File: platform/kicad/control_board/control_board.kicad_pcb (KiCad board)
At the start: 2 copper layers, 81.5 x 131.5 mm, 63 parts, among them J1 DHT22, J10 ADC1,7, J11 Qwiic JST, J12 Conn_01x03, J13 PJ-002A, J14 ROUTER 24V, J15 24V/5V OUT, J16 Conn_01x05_Pin, J2 DS18B20, J3 Conn_01x03, J4 24V IN, J5 USB4120-03-C_REVA, J8 UART, J9 ADC1,6, K1 LCA717, K2 LCA717, K3 LCA717, K4 LCA717, U1 ESP32-DevKitC, U2 ACS722xLCTR-20AU, U3 AP63205WU-7

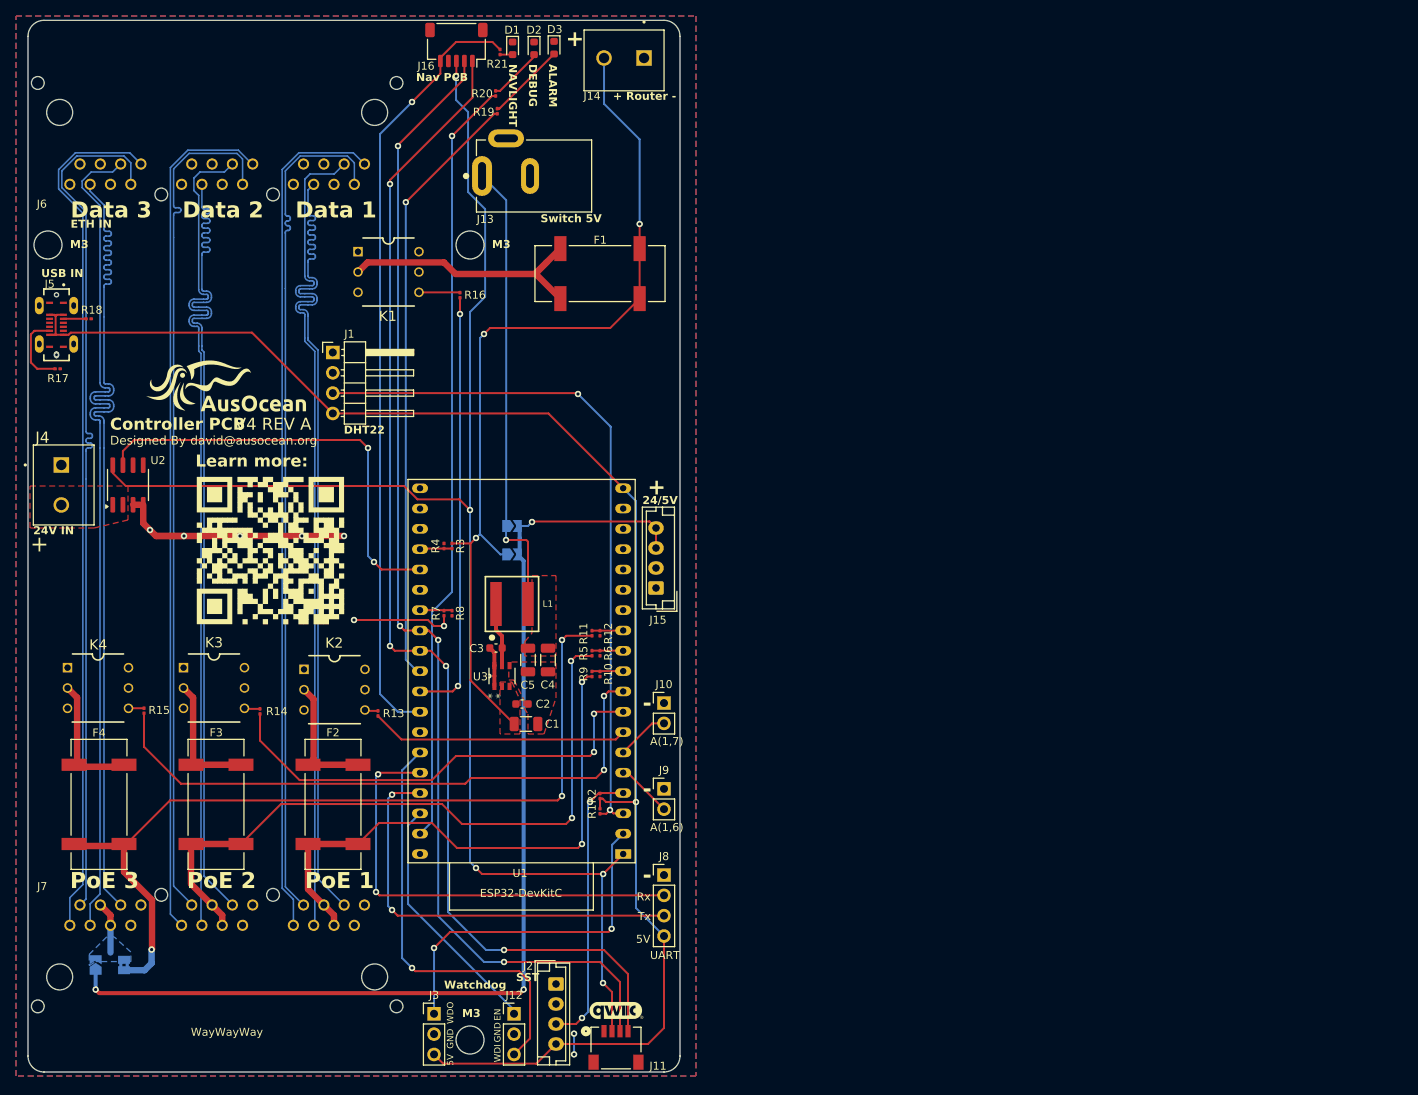
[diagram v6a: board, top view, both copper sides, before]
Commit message: Control_PCB v4 revB: Finalised Design
This change updates the controller PCB to a finalised state, only requiring
finishing touches to be made for manufacturing.
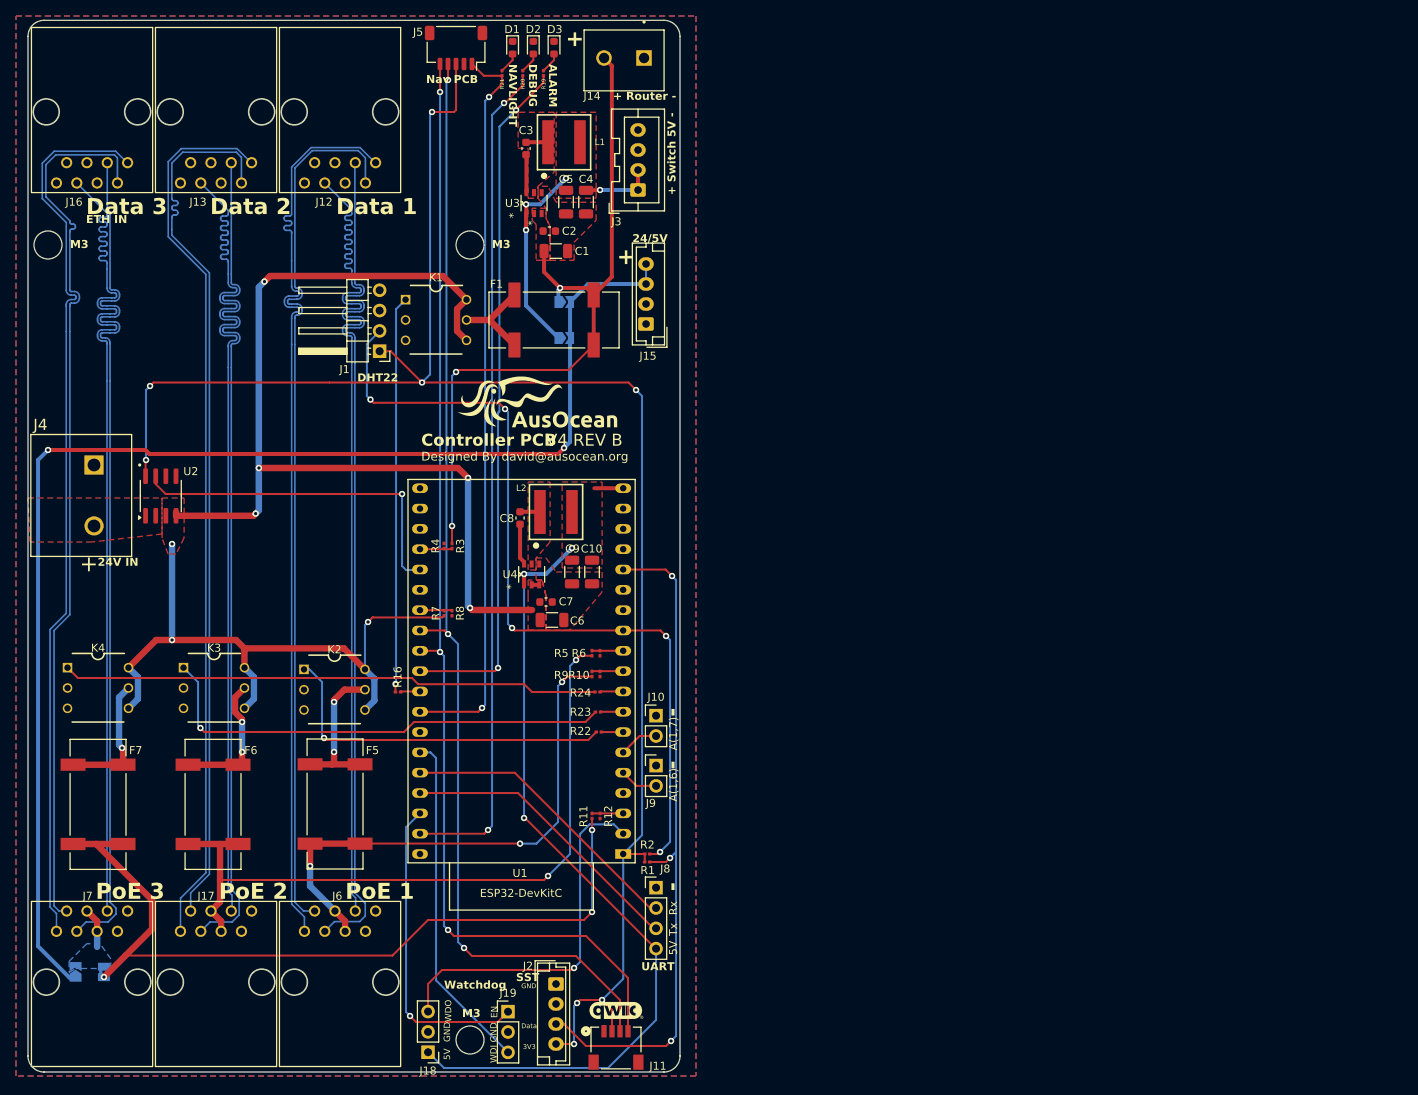
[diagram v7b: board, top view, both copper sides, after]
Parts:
- removed F2, F3, F4: 3588TR, AusOcean:3588TR_FUSE_HOLDER
- removed R13, R14, R15: 2.2K, Resistor_SMD:R_0201_0603Metric
- removed R17, R18: 5.1K, Resistor_SMD:R_0201_0603Metric
- added C10: 22u, Capacitor_SMD:C_1206_3216Metric, F.Cu at (156.2, 94.2)
- added C6: 10u, Capacitor_SMD:C_1206_3216Metric, F.Cu at (151.2, 100.2)
- added C7: 0.1u, Capacitor_SMD:C_0603_1608Metric, F.Cu at (150.4, 97.9)
- added C8: 0.1u, Capacitor_SMD:C_0603_1608Metric, F.Cu at (147.2, 87.4)
- added C9: 22u, Capacitor_SMD:C_1206_3216Metric, F.Cu at (153.7, 94.2)
- added F5: 3588TR, AusOcean:3588TR_FUSE_HOLDER, F.Cu at (124.1, 123.2)
- added F6: 3588TR, AusOcean:3588TR_FUSE_HOLDER, F.Cu at (108.8, 123.2)
- added F7: 3588TR, AusOcean:3588TR_FUSE_HOLDER, F.Cu at (94.4, 123.2)
- added J17: PoE 2, AusOcean:CONNFLY Elec DS1128-05-S8B8P, F.Cu at (109.2, 136.5)
- added J18: Conn_01x03, Connector_PinHeader_2.54mm:PinHeader_1x03_P2.54mm_Vertical, F.Cu at (135.7, 154.2)
- added J19: Conn_01x03, Connector_PinHeader_2.54mm:PinHeader_1x03_P2.54mm_Vertical, F.Cu at (145.7, 149.1)
- added L2: 6.8u, AusOcean:WE-XHMI_6060, F.Cu at (151.7, 86.7)
- added R22: 2.2K, Resistor_SMD:R_0201_0603Metric, F.Cu at (157.0, 114.2)
- added R23: 2.2K, Resistor_SMD:R_0201_0603Metric, F.Cu at (156.9, 111.7)
- added R24: 2.2K, Resistor_SMD:R_0201_0603Metric, F.Cu at (156.9, 109.2)
- added U4: AP63205WU-7, AusOcean:SOIC_05WU-7_DIO, F.Cu at (148.6, 94.5)
- J12: value Conn_01x03 -> Data 1; footprint Connector_PinHeader_2.54mm:PinHeader_1x03_P2.54mm_Vertical -> AusOcean:CONNFLY Elec DS1128-05-S8B8P
- J13: value PJ-002A -> Data 2; footprint AusOcean:CUI_PJ-002A -> AusOcean:CONNFLY Elec DS1128-05-S8B8P
- J16: value Conn_01x05_Pin -> Data 3; footprint Connector_JST:JST_SH_SM05B-SRSS-TB_1x05-1MP_P1.00mm_Horizontal -> AusOcean:CONNFLY Elec DS1128-05-S8B8P
- J3: value Conn_01x03 -> Conn_01x04; footprint Connector_PinHeader_2.54mm:PinHeader_1x03_P2.54mm_Vertical -> Connector_JST:JST_XA_B04B-XASK-1_1x04_P2.50mm_Vertical
- J4: footprint AusOcean:CUI_Screw_terminal_1x2 -> AusOcean:CUI_TB005-762-02BE
- J5: value USB4120-03-C_REVA -> Conn_01x05_Pin; footprint AusOcean:GCT_USB4120-03-C_REVA -> Connector_JST:JST_SH_SM05B-SRSS-TB_1x05-1MP_P1.00mm_Horizontal
- J6: value ~ -> PoE 1; footprint AusOcean:RJ45 3-port jack -> AusOcean:CONNFLY Elec DS1128-05-S8B8P
- J7: value ~ -> PoE 3; footprint AusOcean:RJ45 3-port jack -> AusOcean:CONNFLY Elec DS1128-05-S8B8P
- K1, K2, K3, K4: footprint AusOcean:LCA717_Relay_Holder -> AusOcean:DIP762W60P254L838H406Q6N
- R1: value 10K -> 4k7
- R2: value 5K -> 4k7
- moved J6 110.9 mm to (124.7, 136.5), turned to 0 degrees
- moved J12 106.1 mm to (124.7, 45.5), turned to 180 degrees
- moved J3 106.1 mm to (161.9, 46.4), turned to 90 degrees
- moved C3 62.6 mm to (147.9, 41.2), turned to 90 degrees
- moved J5 60.8 mm to (139.2, 28.7), turned to 180 degrees
- moved U3 59.2 mm to (148.9, 48.1)
- moved C1 59.2 mm to (151.7, 54.1)
- moved C2 59.2 mm to (150.9, 51.6)
- moved L1 58.1 mm to (152.7, 40.5)
- moved C4 57.4 mm to (155.4, 47.9)
- moved C5 57.4 mm to (152.9, 47.9)
- moved R16 50.2 mm to (131.9, 109.2), turned to 0 degrees
- moved J16 48.7 mm to (93.7, 45.5)
- moved G*** 39.0 mm to (149.3, 72.9)
- moved J13 33.3 mm to (109.2, 45.5), turned to 180 degrees
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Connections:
- F1 pad 3: Net-(K1--_LOAD) -> Net-(K1-LOAD-)
- F1 pad 4: Net-(K1--_LOAD) -> Net-(K1-LOAD-)
- J1 pad 1: GND -> +3V3
- J1 pad 2: unconnected-(J1-Pin_2-Pad2) -> DHT
- J1 pad 3: DHT -> unconnected-(J1-Pin_3-Pad3)
- J1 pad 4: 5VIN -> GND
- J12 pad 1: WD_EN* -> D1_Rx+
- J12 pad 2: GND -> D1_Rx-
- J12 pad 3: WD_IN -> D1_Tx+
- J13 pad 1: NW_5V -> D2_Rx+
- J13 pad 2: GND -> D2_Rx-
- J13 pad 3: unconnected-(J13-Pad3) -> D2_Tx+
- J16 pad 1: SCL -> D3_Rx+
- J16 pad 2: SDA -> D3_Rx-
- J16 pad 3: +3V3 -> D3_Tx+
- J16 pad 4: GND -> unconnected-(J16-Pad4)
- J16 pad 5: Navlight -> unconnected-(J16-Pad5)
- J2 pad 4: 5VIN -> +3V3
- J3 pad 1: EN -> NW_5V
- J3 pad 2: GND -> NW_5V
- J3 pad 3: 5VIN -> GND
- J6 pad 4: unconnected-(J6-Pad4) -> P1_out
- J6 pad 5: unconnected-(J6-Pad5) -> P1_out
- J6 pad 7: unconnected-(J6-Pad7) -> GND
- J6 pad 8: unconnected-(J6-Pad8) -> GND
- K1 pad 1: 24VIN -> Net-(K1-+CONTROL)
- K1 pad 2: Net-(K1--_LOAD) -> GND
- K1 pad 3: 24VIN -> unconnected-(K1-NC-Pad3)
- K1 pad 4: Net-(K1-+_CONTROL) -> 24VIN
- K1 pad 5: GND -> Net-(K1-LOAD-)
- K1 pad 6: unconnected-(K1-DO_NOT_USE-Pad6) -> 24VIN
- K2 pad 1: 24VIN -> Net-(K2-+CONTROL)
- K2 pad 2: Net-(K2--_LOAD) -> GND
- K2 pad 3: 24VIN -> unconnected-(K2-NC-Pad3)
- K2 pad 4: Net-(K2-+_CONTROL) -> 24VIN
- K2 pad 5: GND -> Net-(K2-LOAD-)
- K2 pad 6: unconnected-(K2-DO_NOT_USE-Pad6) -> 24VIN
- K3 pad 1: 24VIN -> Net-(K3-+CONTROL)
- K3 pad 2: Net-(K3--_LOAD) -> GND
- K3 pad 3: 24VIN -> unconnected-(K3-NC-Pad3)
- K3 pad 4: Net-(K3-+_CONTROL) -> 24VIN
- K3 pad 5: GND -> Net-(K3-LOAD-)
- K3 pad 6: unconnected-(K3-DO_NOT_USE-Pad6) -> 24VIN
- K4 pad 1: 24VIN -> Net-(K4-+CONTROL)
- K4 pad 2: Net-(K4--_LOAD) -> GND
- K4 pad 3: 24VIN -> unconnected-(K4-NC-Pad3)
- K4 pad 4: Net-(K4-+_CONTROL) -> 24VIN
- K4 pad 5: GND -> Net-(K4-LOAD-)
- K4 pad 6: unconnected-(K4-DO_NOT_USE-Pad6) -> 24VIN
- R1 pad 2: 5VIN -> +3V3
- R16 pad 1: Net-(K1-+_CONTROL) -> Net-(K1-+CONTROL)
- R2 pad 2: 5VIN -> +3V3
- U1 pad 12: _P3_out -> DHT
- U1 pad 13: _P4_out -> unconnected-(U1-MTDI/GPIO12/ADC2_CH5-Pad13)
- U1 pad 15: Power 4 -> SST
- U1 pad 3: DHT -> _P3_out
- U1 pad 4: SST -> unconnected-(U1-SENSOR_VN/GPIO39/ADC1_CH3-Pad4)
- U3 pad 1: Net-(U3-BST) -> NW_5V
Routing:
- net 24VIN: track 45.6 -> 205.7 mm, vias 7 -> 8
- net 5VIN: track 190.9 -> 106.8 mm, vias 1 -> 3
- net Power 3: track 76.2 -> 2.92 mm, vias 2 -> 0
- net Net-(K4-+CONTROL): track 0.00 -> 67.2 mm
- net Net-(K3-+CONTROL): track 0.00 -> 59.0 mm, vias 0 -> 1
- net Power 2: track 57.1 -> 2.84 mm, vias 2 -> 0
- net NW: track 53.7 -> 2.45 mm, vias 2 -> 0
- net Net-(K1-+CONTROL): track 0.00 -> 49.6 mm, vias 0 -> 1
- net SST: track 35.6 -> 85.1 mm, vias 2 -> 3
- net Net-(K2-+CONTROL): track 0.00 -> 44.6 mm, vias 0 -> 1
- net Net-(K1--_LOAD): track 34.1 -> 0.00 mm
- net 5-24VOUT: track 134.6 -> 165.4 mm, vias 3 -> 2
- net Power 1: track 32.9 -> 2.73 mm
- net +3V3: track 190.9 -> 220.5 mm, vias 5 -> 8
- net NW_5V: track 57.4 -> 33.8 mm, vias 1 -> 4
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- added copper zone on F.Cu, net 24VIN
- added copper zone on F.Cu, net 5VIN
- added copper zone on F.Cu, net Net-(U3-SW)
- added copper zone on F.Cu, net Net-(U4-SW)
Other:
- board text added: "+ Switch 5V -"
- board text added: "1. Not using additional power - Do nothing 2. Using 24/5V JST (J15) - Select 24V or 5V using JP1 and JP2 3. Using PoE 3 for PoE network device - Select 24V or 5V using JP1 and JP2 - Cut JP3 and solder JP4"
- board text added: "3V3"
- board text added: "Data"
- board text added: "Select only 24V (JP1) OR 5V (JP2)"
- board text added: "V4 REV B"
- board text removed: "1. Not using additional power - Do nothing 2. Using 24/5V JST (J12) - Select 24V or 5V using JP1 and JP2 3. Using PoE 3 for PoE network device - Select 24V or 5V using JP1 and JP2 - Cut JP3 and solder JP4"
- board text removed: "Disable External Watchdog"
- board text removed: "Learn more:"
- board text removed: "Select only 5V (JP2) OR 24V (JP1)"
- board text removed: "Switch 5V"
- board text removed: "USB IN"
- board text removed: "V4 REV A"
- board text removed: "WayWayWay"
